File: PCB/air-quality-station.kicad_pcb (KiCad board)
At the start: 4 copper layers, 50 x 50 mm, 62 parts, among them J1 USB_C_Receptacle_USB2.0_16P, J2 UART, J3 I2C_3, J4 SEN55, J5 I2C_1, J6 I2C_2, J7 I2C_4, J9 E-Paper, Q1 Si1308EDL, U1 ESP32-C6-MINI-1/U, U2 SCD41-D-R2, U3 BMP280, U4 TLV73333PDBV, U6 USBLC6-2P6, U7 TLV73333PDBV, U8 TLV73333PDBV, Y1 32.768kHz

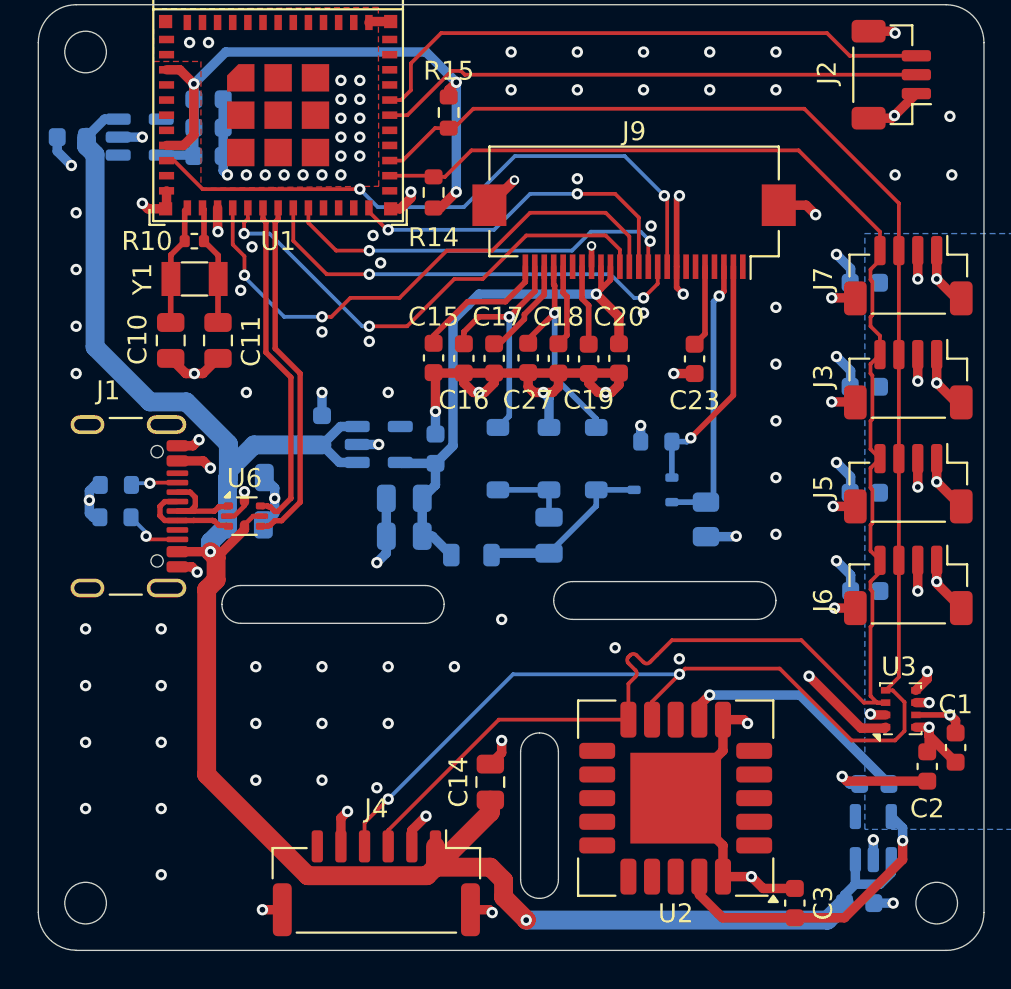
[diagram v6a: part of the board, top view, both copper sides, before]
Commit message: Improved LDOs, dropped one extension port
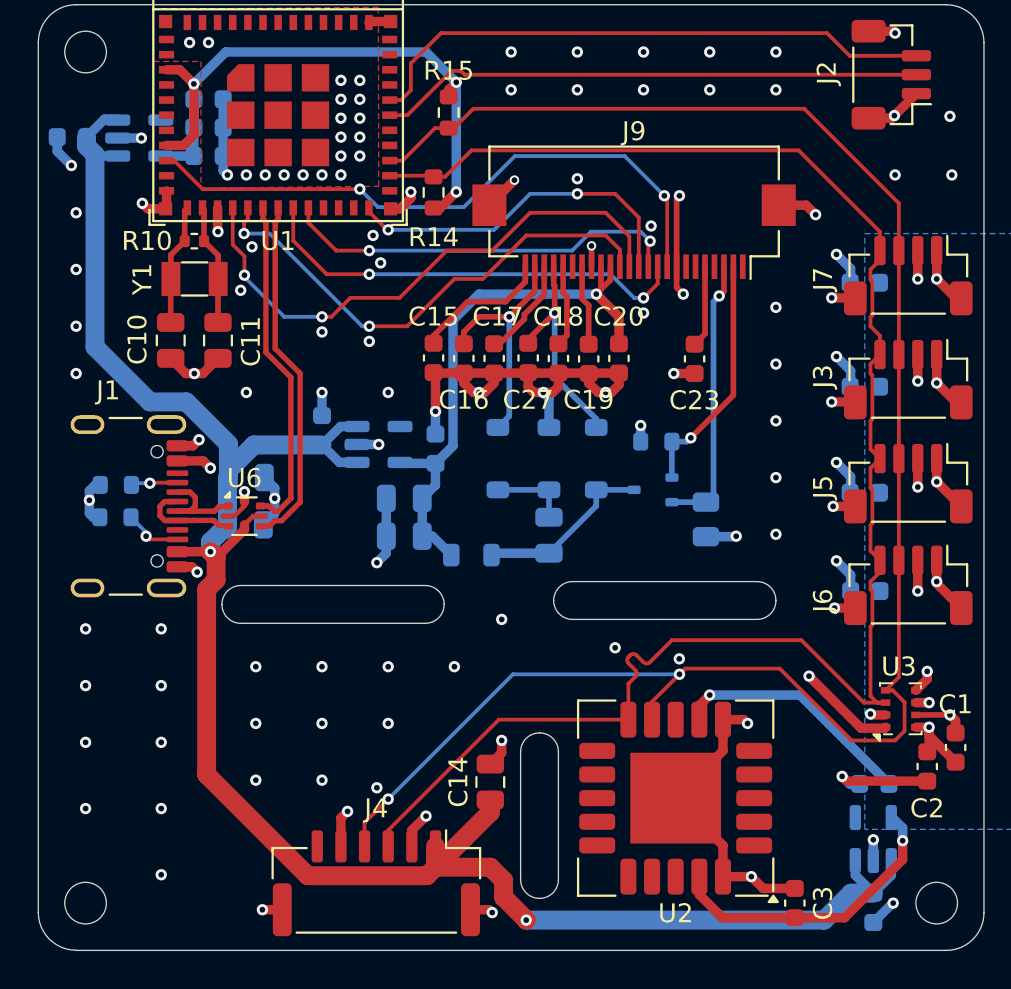
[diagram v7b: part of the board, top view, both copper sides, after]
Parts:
- removed U8: TLV73333PDBV, Package_TO_SOT_SMD:SOT-23-5
- added U5: TLV75533PDBV, Package_TO_SOT_SMD:SOT-23-5, B.Cu at (50.8, 56.5)
- C4, C5: value 100nF -> 1uF
- U4, U7: value TLV73333PDBV -> TLV75533PDBV
- moved U7 20.6 mm to (63.5, 72.8)
- moved C4 0.79 mm to (89.7, 97.2), turned to -90 degrees
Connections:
- U7 pad 5: +3V3_MCU -> +3V3_DISP
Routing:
- net +5V: track 108.4 -> 110.2 mm
